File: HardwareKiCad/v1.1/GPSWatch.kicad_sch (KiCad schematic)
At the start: 58 parts, among them J1 USB_B_Micro, J2 Battery, J4 Micro_SD_Card_Det2, J5 Conn_01x04_Pin, SW1 EC05E1220401, SW2 SW_SPDT, SW3 SW_Push, SW4 SW_Push, SW5 SW_Push, U1 STM32F103C8Tx, U3 MCP73831-2-OT, U4 TPS2116DRL, U5 L96-M33, U6 BMA456, U7 AMS1117CS-3.3, Y1 ABM3-8.000MHZ-B4Y-T

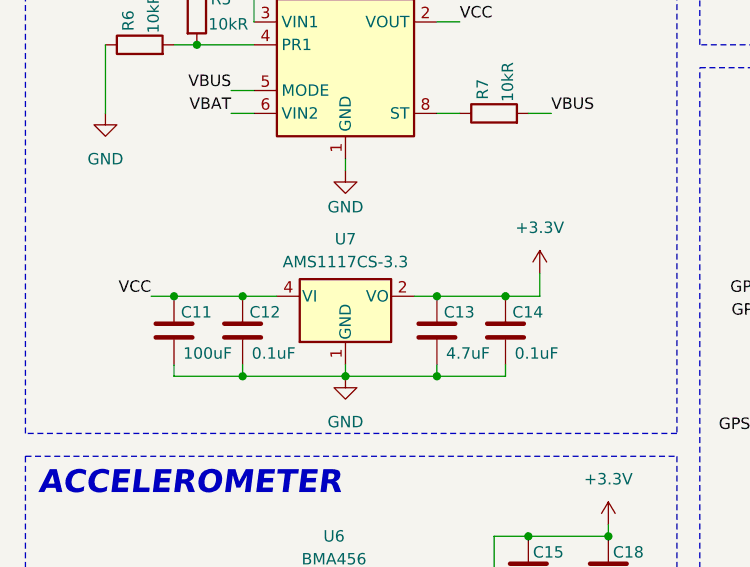
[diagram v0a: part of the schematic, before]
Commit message: Change MCP 73831 from SOIC 8 to SOT 223
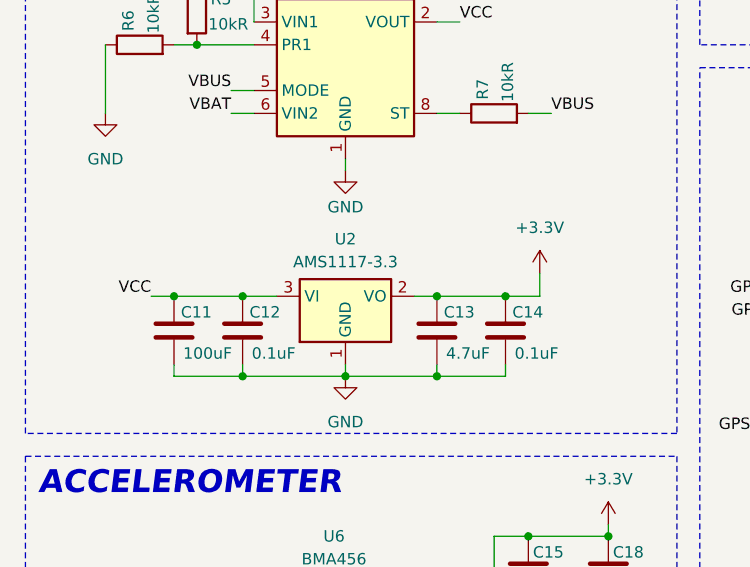
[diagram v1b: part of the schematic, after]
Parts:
- removed U7: AMS1117CS-3.3, Package_SO:SOIC-8_3.9x4.9mm_P1.27mm, symbol Regulator_Linear:AMS1117CS-3.3
- added U2: AMS1117-3.3, Package_TO_SOT_SMD:SOT-223-3_TabPin2, symbol Regulator_Linear:AMS1117-3.3
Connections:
- net +3.3V: now also U2.2 (VO)
- net GND: now also U2.1 (GND)
- net VCC: now also U2.3 (VI)
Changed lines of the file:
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@@
 	)
 	(symbol
+		(lib_id "Regulator_Linear:AMS1117-3.3")
+		(at 49.53 90.17 0)
+		(unit 1)
+		(exclude_from_sim no)
+		(in_bom yes)
+		(on_board yes)
+		(dnp no)
+		(fields_autoplaced yes)
+		(property "Reference" "U2"
+			(at 49.53 83.82 0)
+			(effects
+				(font
+					(size 1.27 1.27)
+				)
+			)
+		)
+		(property "Value" "AMS1117-3.3"
+			(at 49.53 86.36 0)
+			(effects
+				(font
+					(size 1.27 1.27)
+				)
+			)
+		)
+		(property "Footprint" "Package_TO_SOT_SMD:SOT-223-3_TabPin2"
+			(at 49.53 85.09 0)
+			(effects
+				(font
+					(size 1.27 1.27)
+				)
+				(hide yes)
+			)
+		)
+		(property "Datasheet" "http://www.advanced-monolithic.com/pdf/ds1117.pdf"
+			(at 52.07 96.52 0)
+			(effects
+				(font
+					(size 1.27 1.27)
+				)
+				(hide yes)
+			)
+		)
+		(property "Description" "1A Low Dropout regulator, positive, 3.3V fixed output, SOT-223"
+			(at 49.53 90.17 0)
+			(effects
+				(font
+					(size 1.27 1.27)
+				)
+				(hide yes)
+			)
+		)
+		(pin "3"
+		)
+		(pin "1"
+		)
+		(pin "2"
+		)
+		(instances
+			(project ""
+				(path "/9f4df342-8db3-41c4-bd1d-44c5477f93e2"
+					(reference "U2")
+					(unit 1)
+				)
+			)
+		)
+	)
+	(symbol
 		(lib_id "Device:C")
 		(at 59.69 93.98 0)
@@
 					(unit 1)
 				)
-			)
-		)
-	)
-	(symbol
-		(lib_id "Regulator_Linear:AMS1117CS-3.3")
-		(at 49.53 90.17 0)
-		(unit 1)
-		(exclude_from_sim no)
-		(in_bom yes)
-		(on_board yes)
-		(dnp no)
-		(fields_autoplaced yes)
-		(property "Reference" "U7"
-			(at 49.53 83.82 0)
-			(effects
-				(font
-					(size 1.27 1.27)
-				)
-			)
-		)
-		(property "Value" "AMS1117CS-3.3"
-			(at 49.53 86.36 0)
-			(effects
-				(font
-					(size 1.27 1.27)
-				)
-			)
-		)
-		(property "Footprint" "Package_SO:SOIC-8_3.9x4.9mm_P1.27mm"
-			(at 49.53 85.09 0)
-			(effects
-				(font
-					(size 1.27 1.27)
-				)
-				(hide yes)
-			)
-		)
-		(property "Datasheet" "http://www.advanced-monolithic.com/pdf/ds1117.pdf"
-			(at 52.07 96.52 0)
-			(effects
-				(font
-					(size 1.27 1.27)
-				)
-				(hide yes)
-			)
-		)
-		(property "Description" "1A Low Dropout regulator, positive, 3.3V fixed output, SOIC-8"
-			(at 49.53 90.17 0)
-			(effects
-				(font
-					(size 1.27 1.27)
-				)
-				(hide yes)
-			)
-		)
-		(pin "3"
-		)
-		(pin "7"
-		)
-		(pin "2"
-		)
-		(pin "5"
-		)
-		(pin "1"
-		)
-		(pin "8"
-		)
-		(pin "4"
-		)
-		(pin "6"
-		)
-		(instances
-			(project ""
-				(path "/9f4df342-8db3-41c4-bd1d-44c5477f93e2"
-					(reference "U7")
-					(unit 1)
-				)
